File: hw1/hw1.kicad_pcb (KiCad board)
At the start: 2 copper layers, 53.9 x 53.3 mm, 35 parts, among them J1 CONN_01X02, J10 TEST_1P, J11 TEST_1P, J2 TEST_1P, J3 TEST_1P, J4 TEST_1P, J5 TEST_1P, J7 TEST_1P, J8 TEST_1P, J9 TEST_1P, P1 Power, P10 CONTROL, P11 CONN_01X06, P2 Analog, P3 Digital, P4 Digital, P9 FX2LA, U1 STM32L151C6TxA, U2 MIC550x-3.3YM5, Y1 Crystal_GND24_Small

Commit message: hw1: more silk cleanup
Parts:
- renumbered J10 to PA0, J11 to PA1, J9 to PA10, J7 to PA8, J8 to PA9, J2 to PB0, J3 to PB1, J4 to PB10, J5 to PB11
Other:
- board text added: "<<<< FX2LA"

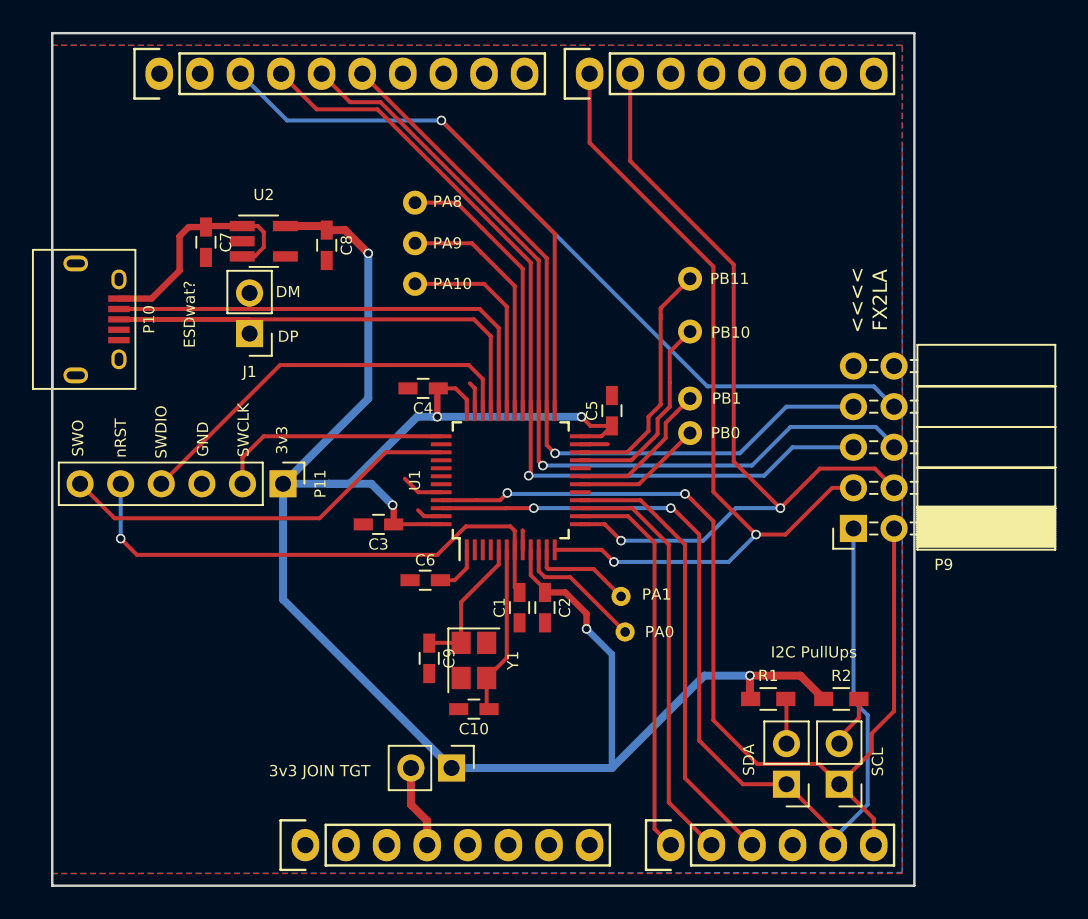
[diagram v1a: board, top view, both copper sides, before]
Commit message: hw1: discover reversed numbering on arduino connectors
joy.  Fixed now against nucleo64 manuals.
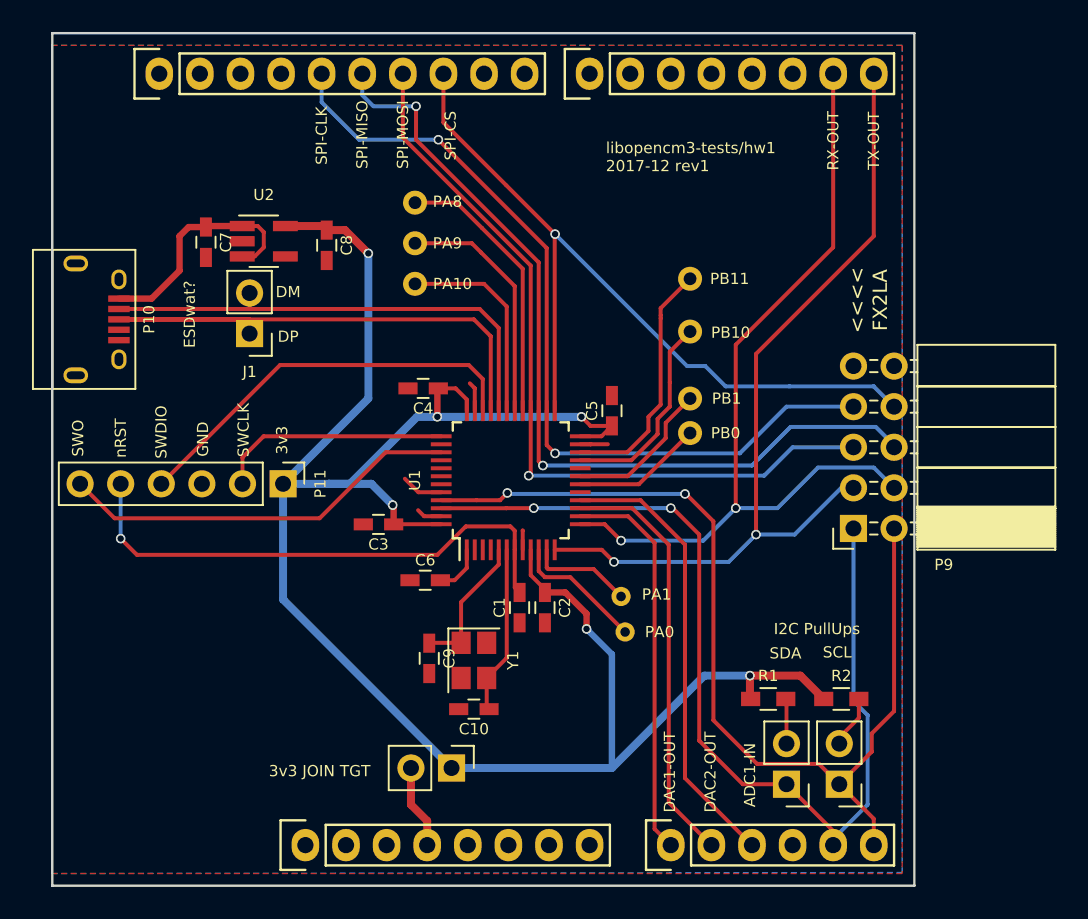
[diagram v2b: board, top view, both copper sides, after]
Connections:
- P3 pad 3: /SPI_CS -> (no net)
- P3 pad 4: /SPI_MOSI -> GND
- P3 pad 5: /SPI_MISO -> /SPI_SCK
- P3 pad 6: /SPI_SCK -> /SPI_MISO
- P3 pad 7: GND -> /SPI_MOSI
- P3 pad 8: (no net) -> /SPI_CS
- P4 pad 1: /UART_TX_OUT -> (no net)
- P4 pad 2: /UART_RX_OUT -> (no net)
- P4 pad 7: (no net) -> /UART_RX_OUT
- P4 pad 8: (no net) -> /UART_TX_OUT
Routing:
- net /SPI_CS: track 70.6 -> 49.7 mm
- net /SPI_MOSI: track 55.0 -> 49.6 mm
- net /SPI_SCK: track 48.6 -> 52.6 mm, vias 1 -> 2
- net /UART_RX_OUT: track 53.5 -> 52.2 mm
- net /UART_TX_OUT: track 54.1 -> 52.8 mm
- net /SPI_MISO: track 54.9 -> 54.3 mm, vias 1 -> 2
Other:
- board text added: "ADC1-IN"
- board text added: "DAC1-OUT"
- board text added: "DAC2-OUT"
- board text added: "RX-OUT"
- board text added: "SPI-CLK"
- board text added: "SPI-CS"
- board text added: "SPI-MISO"
- board text added: "SPI-MOSI"
- board text added: "TX-OUT"
- board text added: "libopencm3-tests/hw1 2017-12 rev1"

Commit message: hw1: termination wat
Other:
- board text added: "Termination? WAT?"
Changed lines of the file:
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@@
   (general
     (links 87)
-    (no_connects 3)
+    (no_connects 24)
     (area 123.024999 72.949999 177.113001 126.440001)
     (thickness 1.6)
-    (drawings 28)
+    (drawings 29)
     (tracks 296)
     (zones 0)
@@
       (rotate (xyz 0 0 270))
     )
+  )
+  (gr_text "Termination?\nWAT?" (at 169.9895 98.4885 90) (layer F.SilkS)
+    (effects (font (size 0.7 0.7) (thickness 0.12)))
   )
   (gr_text "libopencm3-tests/hw1\n2017-12 rev1" (at 157.734 80.772) (layer F.SilkS)
@@
     (connect_pads (clearance 0.508))
     (min_thickness 0.254)
-    (fill yes (arc_segments 16) (thermal_gap 0.508) (thermal_bridge_width 0.508))
+    (fill (arc_segments 16) (thermal_gap 0.508) (thermal_bridge_width 0.508))
     (polygon
       (pts
@@
     (connect_pads (clearance 0.25))
     (min_thickness 0.25)
-    (fill yes (arc_segments 16) (thermal_gap 0.25) (thermal_bridge_width 0.3))
+    (fill (arc_segments 16) (thermal_gap 0.25) (thermal_bridge_width 0.3))
     (polygon
       (pts
